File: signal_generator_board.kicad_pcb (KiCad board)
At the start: 2 copper layers, 100 x 43.8 mm, 50 parts, among them IC1 CD4001, IC2 CD4017, IC3 CD4017, IC4 MAX297, IC5 MCP6024, IC6 NE5532, IC7 ATMEG328PU, IC8 LTC6903/4, IC9 AD5207, P1 CONN_10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

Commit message: v1.0
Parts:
- removed IC2, IC3: CD4017, SO16E
- removed IC4: MAX297, SO8E
- removed IC9: AD5207, TSSOP14
- removed R4: 2.5Meg, SM1206
- removed R5: 1.5Meg, SM1206
- removed R6, R7: 10k, SM1206
- removed RES1: 16MHz, PIN_ARRAY_3X1
- added C17: 0.1uF, SM0603, F.Cu at (106.5, 61.9)
- added C18: 0.1uF, SM0603, F.Cu at (106.0, 45.6)
- added JP1: USB_POWER, PIN_ARRAY_2X1, F.Cu at (110.8, 31.7)
- added Q1: 2N7002, SOT23, F.Cu at (91.7, 47.0)
- added U1: 4066, SO14E, F.Cu at (90.5, 57.7)
- added U2: 74LS393, SO14E, F.Cu at (118.2, 58.5)
- added X1: 16MHz, HC-49V, F.Cu at (95.1, 29.6)
- C10, C11: value 1uF -> 22pF
- C12: value 0.1uF -> 1uF; footprint SM0603 -> SM1206
- C13: value 1uF -> 5pF
- C3: value 0.1uF -> 47nF; footprint SM0603 -> SM1206
- C4: value 0.1uF -> 470pF; footprint SM0603 -> SM1206
- C6: value 0.1uF -> 6.8nF; footprint SM0603 -> SM1206
- C7: value 1uF -> 68pF
- IC1: value CD4001 -> AD5206; footprint SO14E -> SO24E
- R2: value 2k -> 1k
- R3: value 3k -> 1Meg
- R8: value 250k -> 25k
- R9: value 1Meg -> 100k
- U3: value RBBB -> TLE2426; footprint RBBB_shield -> SO8E
- moved D1 89.3 mm to (29.4, 60.2), turned to 0 degrees
- moved R10 89.2 mm to (29.7, 57.6), turned to 0 degrees
- moved C10 45.0 mm to (105.1, 29.9)
- moved P6 42.9 mm to (81.9, 29.7), turned to 180 degrees
- moved R3 34.2 mm to (102.5, 29.9), turned to 90 degrees
- moved C3 32.4 mm to (86.8, 64.6), turned to 90 degrees
- moved SW1 32.4 mm to (120.2, 37.3), turned to 270 degrees
- moved U3 31.9 mm to (109.9, 64.3), turned to 0 degrees
- moved C11 31.4 mm to (87.7, 29.8)
- moved C8 23.3 mm to (120.7, 62.8)
- moved R1 21.4 mm to (118.8, 31.1)
- moved C14 20.7 mm to (113.6, 66.6), turned to 90 degrees
- moved C4 17.6 mm to (89.5, 64.6), turned to 90 degrees
- moved C5 16.4 mm to (84.7, 57.7), turned to 90 degrees
- moved IC5 16.1 mm to (100.7, 64.1)
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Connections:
- net +3.3V_SCL renamed N-0000016
- net +3.3V_SDA renamed N-0000013
- C10 pad 1: N-0000081 -> GND
- C10 pad 2: N-0000082 -> N-0000071
- C11 pad 1: N-0000082 -> GND
- C11 pad 2: 5Vp-p_WAVEOUT -> N-0000072
- C12 pad 1: N-0000048 -> N-0000040
- C12 pad 2: G -> 5Vp-p_WAVEOUT
- C14 pad 2: G -> GND
- C15 pad 2: G -> GND
- C16 pad 1: +12V -> GND
- C16 pad 2: G -> +12V
- C2 pad 2: G -> GND
- C3 pad 1: +5V -> C1A
- C3 pad 2: G -> N-000006
- C4 pad 1: +5V -> C1A
- C4 pad 2: G -> N-000001
- C5 pad 1: +5V -> GND
- C5 pad 2: G -> +5V
- C6 pad 1: +5V -> C2A
- C6 pad 2: G -> N-000004
- C7 pad 1: N-0000040 -> C2A
- C8 pad 1: VGND -> GND
- C8 pad 2: G -> +5V
- C9 pad 2: G -> GND
- D1 pad 2: G -> GND
- IC1 pad 1: N-0000078 -> N-0000025
- IC1 pad 10: (no net) -> N-0000020
- IC1 pad 11: (no net) -> N-0000025
- IC1 pad 12: G -> N-0000025
- IC1 pad 13: G -> C1A
- IC1 pad 14: +5V -> C2A
- IC1 pad 2: N-0000083 -> N-0000041
- IC1 pad 3: N-0000079 -> VGND
- IC1 pad 4: N-0000083 -> GND
- IC1 pad 5: N-0000079 -> D3
- IC1 pad 6: /CLK -> +5V
- IC1 pad 7: G -> D11/MOSI
- IC1 pad 8: G -> D13/SCK
- IC1 pad 9: G -> GND
- IC5 pad 1: N-0000082 -> C1B
- IC5 pad 10: VGND -> N-0000041
- IC5 pad 11: G -> GND
- IC5 pad 13: N-0000063 -> N-0000020
- IC5 pad 14: N-0000063 -> N-0000025
- IC5 pad 2: N-0000081 -> C1B
- IC5 pad 3: (no net) -> C2A
- IC5 pad 5: N-0000048 -> N-0000042
- IC5 pad 6: VGND -> N-0000044
- IC5 pad 7: VGND -> N-0000044
- IC5 pad 8: N-0000061 -> 5Vp-p_WAVEOUT
- IC5 pad 9: N-0000061 -> 5Vp-p_WAVEOUT
- IC6 pad 3: G -> GND
- IC6 pad 5: G -> GND
- IC7 pad 10: N-0000021 -> N-0000072
- IC7 pad 11: D5 -> (no net)
- IC7 pad 12: D6 -> (no net)
- IC7 pad 13: D7 -> (no net)
- IC7 pad 14: D8 -> (no net)
- IC7 pad 15: D9 -> (no net)
- IC7 pad 16: D10 -> (no net)
- IC7 pad 20: G -> +5V
- IC7 pad 21: AR -> (no net)
- IC7 pad 22: +5V -> GND
- IC7 pad 23: A0 -> (no net)
- IC7 pad 24: A1 -> (no net)
- IC7 pad 25: A2 -> (no net)
- IC7 pad 26: A3 -> (no net)
- IC7 pad 8: G -> GND
- IC7 pad 9: N-0000019 -> N-0000071
- IC8 pad 1: G -> GND
- IC8 pad 6: /CLK -> N-0000045
- P1 pad 3: G -> GND
- P1 pad 8: G -> N-0000015
- P1 pad 9: +3.3V -> N-0000014
- P2 pad 3: +3.3V -> (no net)
- P2 pad 5: G -> GND
- P2 pad 6: G -> GND
- P2 pad 7: G -> GND
- P2 pad 8: G -> GND
- P3 pad 1: G -> GND
- P3 pad 3: +5V -> +5V_USB
- P4 pad 3: G -> GND
- P4 pad 8: G -> N-0000015
- P4 pad 9: +3.3V -> N-0000014
- P5 pad 1: G -> GND
- P6 pad 6: G -> GND
- R2 pad 1: N-0000069 -> +5V
- R2 pad 2: N-0000059 -> N-000007
- R3 pad 1: N-0000059 -> N-0000071
- R3 pad 2: VGND -> N-0000072
- R8 pad 1: 5Vp-p_WAVEOUT -> N-0000040
- SW1 pad 2: G -> GND
- SW1 pad 4: G -> GND
- U3 pad 1: RST -> VGND
- U3 pad 2: G -> GND
- U3 pad 4: TX -> (no net)
- U3 pad 5: RX -> (no net)
- U3 pad 6: D2 -> (no net)
- U3 pad 7: D3 -> (no net)
- U3 pad 8: D4 -> N-0000038
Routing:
- net G: track 216.7 -> 0.00 mm, vias 7 -> 0
- net GND: track 0.00 -> 126.3 mm, vias 0 -> 5
- net +3.3V: track 81.9 -> 0.00 mm
- net N-0000014: track 0.00 -> 49.3 mm
- net /CLK: track 46.2 -> 0.00 mm
- net N-0000015: track 0.00 -> 43.3 mm
- net C1B: track 0.00 -> 39.6 mm, vias 0 -> 4
- net N-0000083: track 38.4 -> 0.00 mm, vias 2 -> 0
- net D4: track 2.54 -> 39.8 mm, vias 0 -> 2
- net N-0000025: track 0.00 -> 34.2 mm, vias 0 -> 2
- net N-0000020: track 0.00 -> 33.7 mm, vias 0 -> 4
- net C1A: track 0.00 -> 31.7 mm, vias 0 -> 2
- net C2A: track 0.00 -> 30.7 mm, vias 0 -> 3
- net N-0000081: track 30.5 -> 0.00 mm
- net 5Vp-p_WAVEOUT: track 27.9 -> 57.5 mm
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- added copper zone on B.Cu, net GND
- added copper zone on F.Cu, net GND
- removed copper zone on B.Cu, net G
- removed copper zone on F.Cu, net G
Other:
- board size 100 x 43.8 mm -> 100 x 44.8 mm
- board text added: "ICSP"
- board text added: "OUT_TO_AMP"

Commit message: Add missing parts to BOM
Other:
- board text added: "Signal Generator Board v1.0.1 http://microfluidics.utoronto.ca/dropbot"
- board text removed: "Signal Generator Board v1.0 http://microfluidics.utoronto.ca/dropbot"
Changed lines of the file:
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@@
     (visible_elements 7FFFFFFF)
     (pcbplotparams
-      (layerselection 284196865)
+      (layerselection 2097152)
       (usegerberextensions true)
       (excludeedgelayer true)
@@
     (effects (font (size 0.8 0.8) (thickness 0.2)))
   )
-  (gr_text "Signal Generator\nBoard v1.0\nhttp://microfluidics.utoronto.ca/dropbot" (at 26.4795 51.562) (layer F.SilkS)
+  (gr_text "Signal Generator\nBoard v1.0.1\nhttp://microfluidics.utoronto.ca/dropbot" (at 26.4795 51.562) (layer F.SilkS)
     (effects (font (size 1.1 0.9) (thickness 0.1875)) (justify left))
   )

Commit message: Fix link on BOM
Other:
- board text added: "Signal Generator Board v1.0.2 http://microfluidics.utoronto.ca/dropbot"
- board text removed: "Signal Generator Board v1.0.1 http://microfluidics.utoronto.ca/dropbot"
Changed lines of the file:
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@@
     (effects (font (size 0.8 0.8) (thickness 0.2)))
   )
-  (gr_text "Signal Generator\nBoard v1.0.1\nhttp://microfluidics.utoronto.ca/dropbot" (at 26.4795 51.562) (layer F.SilkS)
+  (gr_text "Signal Generator\nBoard v1.0.2\nhttp://microfluidics.utoronto.ca/dropbot" (at 26.4795 51.562) (layer F.SilkS)
     (effects (font (size 1.1 0.9) (thickness 0.1875)) (justify left))
   )

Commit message: Add paste and pos files
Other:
- board text added: "Signal Generator Board v1.0 http://microfluidics.utoronto.ca/dropbot"
- board text removed: "Signal Generator Board v1.0.2 http://microfluidics.utoronto.ca/dropbot"
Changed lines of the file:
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@@
     (visible_elements 7FFFFFFF)
     (pcbplotparams
-      (layerselection 2097152)
+      (layerselection 284983297)
       (usegerberextensions true)
       (excludeedgelayer true)
@@
     (effects (font (size 0.8 0.8) (thickness 0.2)))
   )
-  (gr_text "Signal Generator\nBoard v1.0.2\nhttp://microfluidics.utoronto.ca/dropbot" (at 26.4795 51.562) (layer F.SilkS)
+  (gr_text "Signal Generator\nBoard v1.0\nhttp://microfluidics.utoronto.ca/dropbot" (at 26.4795 51.562) (layer F.SilkS)
     (effects (font (size 1.1 0.9) (thickness 0.1875)) (justify left))
   )

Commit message: Change C4 and C7 (update BOM)
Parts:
- C4: value 470pF -> 4.7nF
- C7: value 68pF -> 680pF
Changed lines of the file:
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@@
       (effects (font (size 0.762 0.762) (thickness 0.127)))
     )
-    (fp_text value 470pF (at 0 0 90) (layer F.SilkS) hide
+    (fp_text value 4.7nF (at 0 0 90) (layer F.SilkS) hide
       (effects (font (size 0.762 0.762) (thickness 0.127)))
     )
@@
       (effects (font (size 0.762 0.762) (thickness 0.127)))
     )
-    (fp_text value 68pF (at 0 0 180) (layer F.SilkS) hide
+    (fp_text value 680pF (at 0 0 180) (layer F.SilkS) hide
       (effects (font (size 0.762 0.762) (thickness 0.127)))
     )

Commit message: Fix #37
Remove DC bias from 5 Vpk-pk output
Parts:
- moved C12 0.23 mm to (82.5, 59.9), turned to 90 degrees
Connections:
- C12 pad 1: N-0000040 (its old number) -> N-0000039
- IC5 pad 8: 5Vp-p_WAVEOUT -> N-0000039
- IC5 pad 9: 5Vp-p_WAVEOUT -> N-0000039
- R8 pad 1: N-0000040 (its old number) -> 5Vp-p_WAVEOUT
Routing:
- net N-0000039: track 0.00 -> 30.7 mm
- net 5Vp-p_WAVEOUT: track 57.5 -> 33.8 mm, vias 1 -> 3
- net N-0000040 (its old number): track 11.5 -> 0.00 mm, vias 2 -> 0
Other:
- board text added: "Signal Generator Board v1.1 http://microfluidics.utoronto.ca/dropbot"
- board text removed: "Signal Generator Board v1.0 http://microfluidics.utoronto.ca/dropbot"

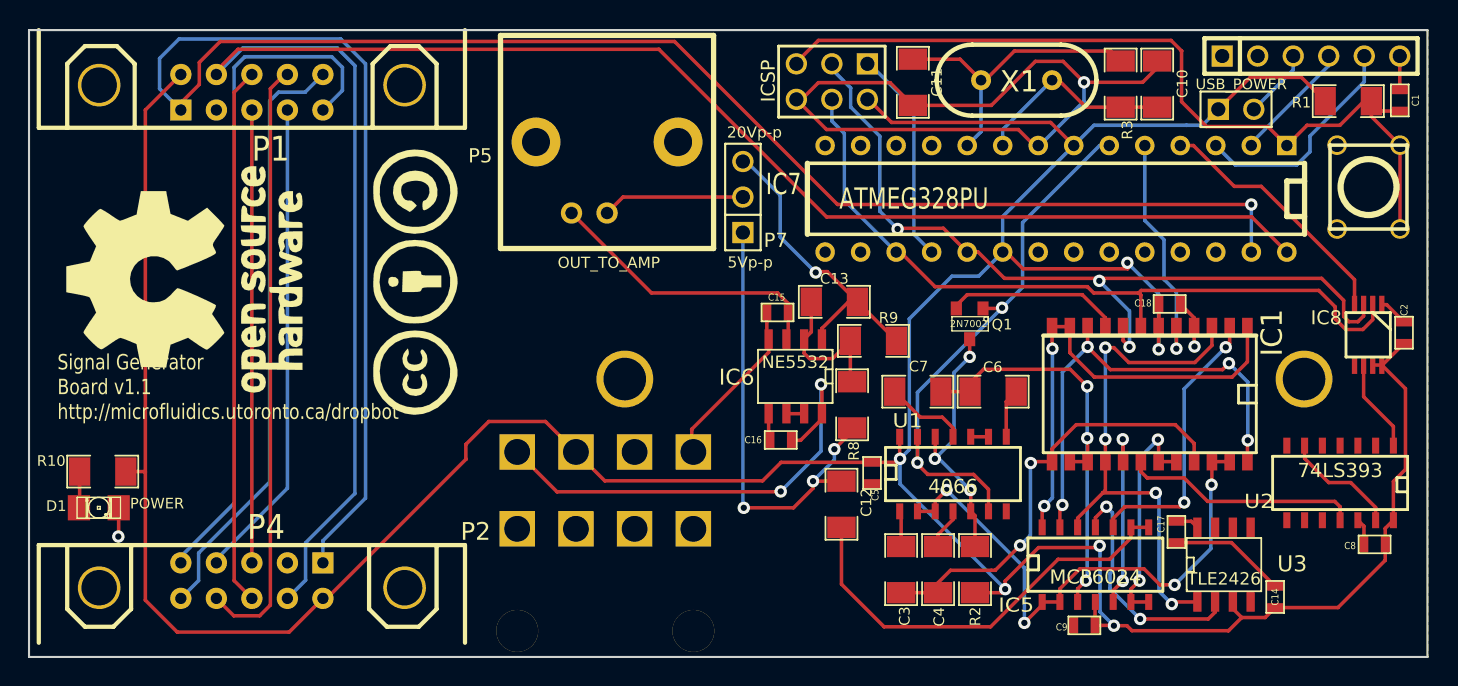
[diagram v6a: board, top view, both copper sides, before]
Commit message: Add ISP prgramming, replace 0603 caps with 1206, ...
* add polarity labels to LEDs
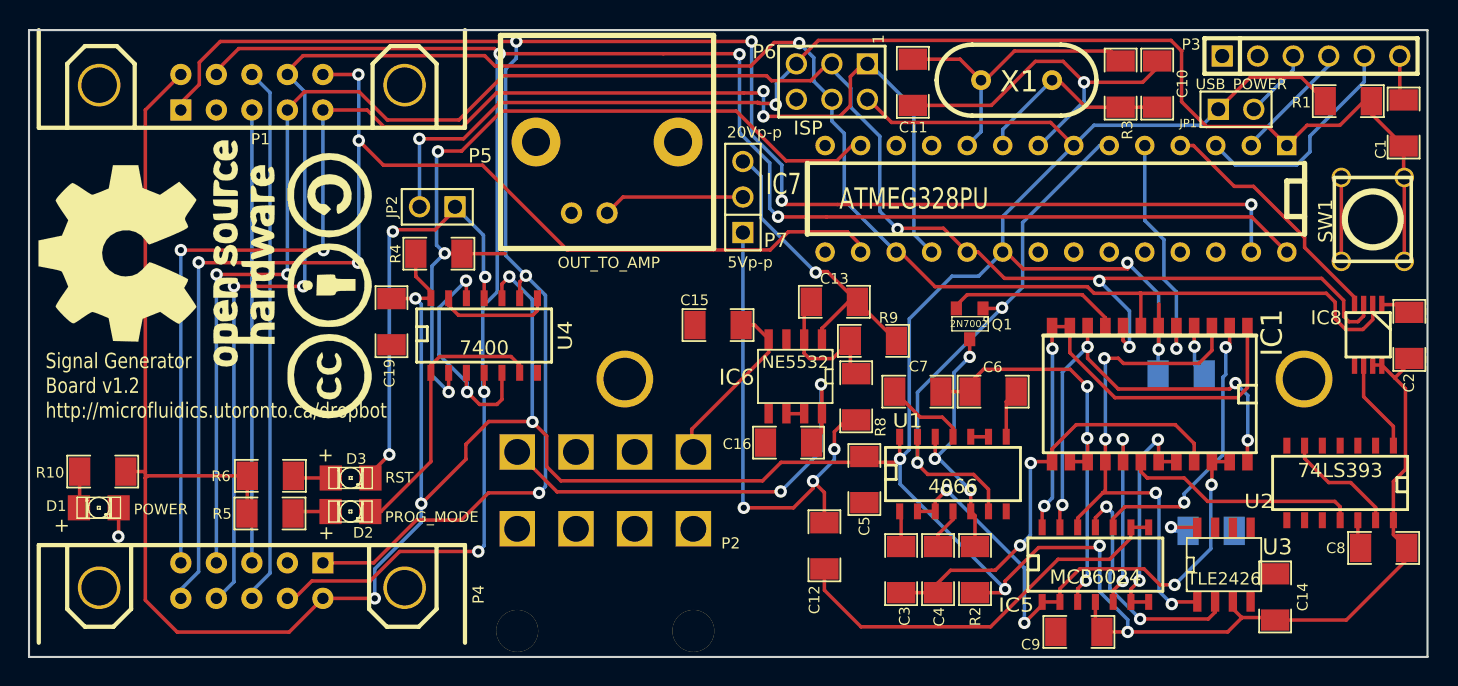
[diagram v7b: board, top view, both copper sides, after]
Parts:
- added C19: 0.1uF, SM1206, F.Cu at (50.4, 46.9)
- added D2: PROG_MODE, LED-1206, F.Cu at (47.4, 60.5)
- added D3: RST, LED-1206, F.Cu at (47.4, 58.1)
- added JP2: JUMPER, PIN_ARRAY_2X1, F.Cu at (53.6, 38.7)
- added R4: 1k, SM1206, F.Cu at (53.8, 42.0)
- added R5: 1k, SM1206, F.Cu at (41.7, 60.6)
- added R6: 1k, SM1206, F.Cu at (41.7, 57.9)
- added U4: 7400, SO14E, F.Cu at (57.0, 47.8)
- C1, C14, C15, C16, C2, C5, C8, C9: footprint SM0603 -> SM1206
- C17, C18: footprint SM0603 -> SM1206; moved to B.Cu
- R10: value 374 -> 1k
- moved G*** 6.14 mm to (45.9, 44.3)
- moved C18 5.11 mm to (106.8, 50.7)
- moved C15 4.35 mm to (73.7, 47.1), turned to 180 degrees
- moved C12 3.21 mm to (81.3, 62.9)
- moved G*** 2.72 mm to (33.6, 42.0)
- moved C17 2.49 mm to (109.0, 61.8), turned to 180 degrees
- moved SW1 2.33 mm to (120.5, 39.6)
- moved C1 1.64 mm to (122.8, 32.7)
- moved C5 0.72 mm to (84.2, 58.2)
- moved C8 0.70 mm to (121.3, 63.1)
- moved R8 0.64 mm to (83.6, 52.3)
- moved C9 0.61 mm to (99.5, 69.1)
- moved C16 0.59 mm to (78.8, 55.5)
- moved C2 0.42 mm to (123.2, 47.9)
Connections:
- C14 pad 1: +5V -> VCC
- C18 pad 1: +5V -> VCC
- C2 pad 1: +5V -> VCC
- C5 pad 2: +5V -> VCC
- C8 pad 2: +5V -> VCC
- C9 pad 1: +5V -> VCC
- IC1 pad 6: +5V -> VCC
- IC5 pad 4: +5V -> VCC
- IC7 pad 13: (no net) -> D7
- IC7 pad 16: (no net) -> D10/SS
- IC7 pad 20: +5V -> VCC
- IC7 pad 7: +5V -> VCC
- IC8 pad 7: +5V -> VCC
- IC8 pad 8: +5V -> VCC
- JP1 pad 1: +5V -> VCC
- P1 pad 10: N-0000013 (its old number) -> D10/SS
- P1 pad 2: +5V -> VCC
- P1 pad 7: N-0000016 -> D13/SCK
- P1 pad 8: N-0000015 (its old number) -> D11/MOSI
- P1 pad 9: N-0000014 -> D12/MISO
- P2 pad 2: +5V -> (no net)
- P4 pad 10: N-0000013 (its old number) -> D10/SS
- P4 pad 2: +5V -> VCC
- P4 pad 7: N-0000016 -> D13/SCK
- P4 pad 8: N-0000015 (its old number) -> D11/MOSI
- P4 pad 9: N-0000014 -> D12/MISO
- P6 pad 2: +5V -> VCC
- R1 pad 2: +5V -> VCC
- R10 pad 2: +5V -> VCC
- R2 pad 1: +5V -> VCC
- U1 pad 14: +5V -> VCC
- U2 pad 14: +5V -> VCC
- U3 pad 3: +5V -> VCC
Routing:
- net VCC: track 0.00 -> 317.2 mm, vias 0 -> 11
- net +5V: track 265.2 -> 0.00 mm, vias 6 -> 0
- net D10/SS: track 0.00 -> 92.6 mm, vias 0 -> 4
- net D12/MISO: track 15.5 -> 103.4 mm, vias 0 -> 4
- net D11/MOSI: track 53.7 -> 140.6 mm, vias 0 -> 3
- net D13/SCK: track 59.2 -> 139.0 mm, vias 3 -> 5
- net D7: track 0.00 -> 57.4 mm, vias 0 -> 3
- net GND: track 126.3 -> 74.2 mm
- net N-0000014: track 49.3 -> 0.00 mm
- net N-0000015 (its old number): track 43.3 -> 0.00 mm
- net N-0000013 (its old number): track 42.8 -> 0.00 mm
- net RST: track 60.8 -> 96.0 mm, vias 0 -> 2
- net N-0000016: track 34.5 -> 0.00 mm
- net N-0000031: track 0.00 -> 31.1 mm, vias 0 -> 3
- net N-0000028: track 0.00 -> 20.1 mm
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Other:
- board text added: "+"
- board text added: "1"
- board text added: "ISP"
- board text added: "Signal Generator Board v1.2 http://microfluidics.utoronto.ca/dropbot"
- board text removed: "ICSP"
- board text removed: "Signal Generator Board v1.1 http://microfluidics.utoronto.ca/dropbot"

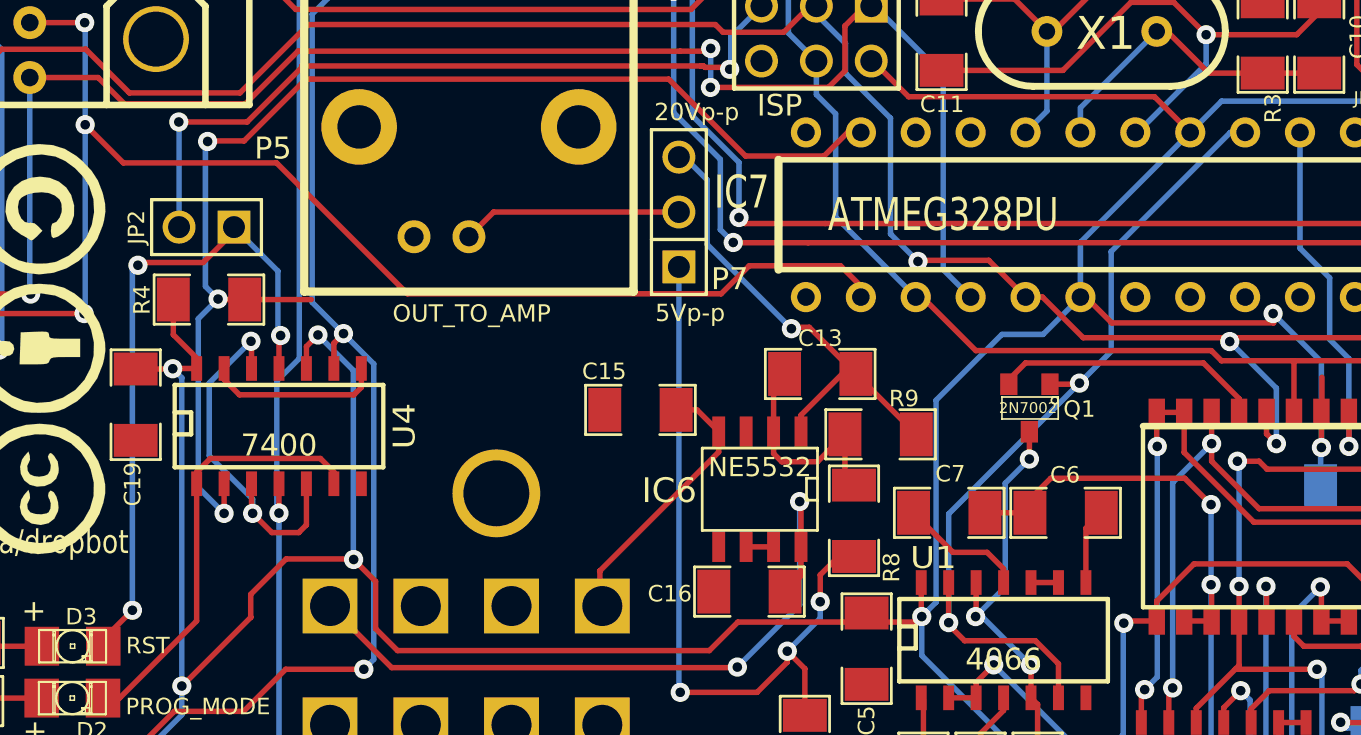
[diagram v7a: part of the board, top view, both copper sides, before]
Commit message: Fix BOM, labels, modify to use soft/bitbanged SPI
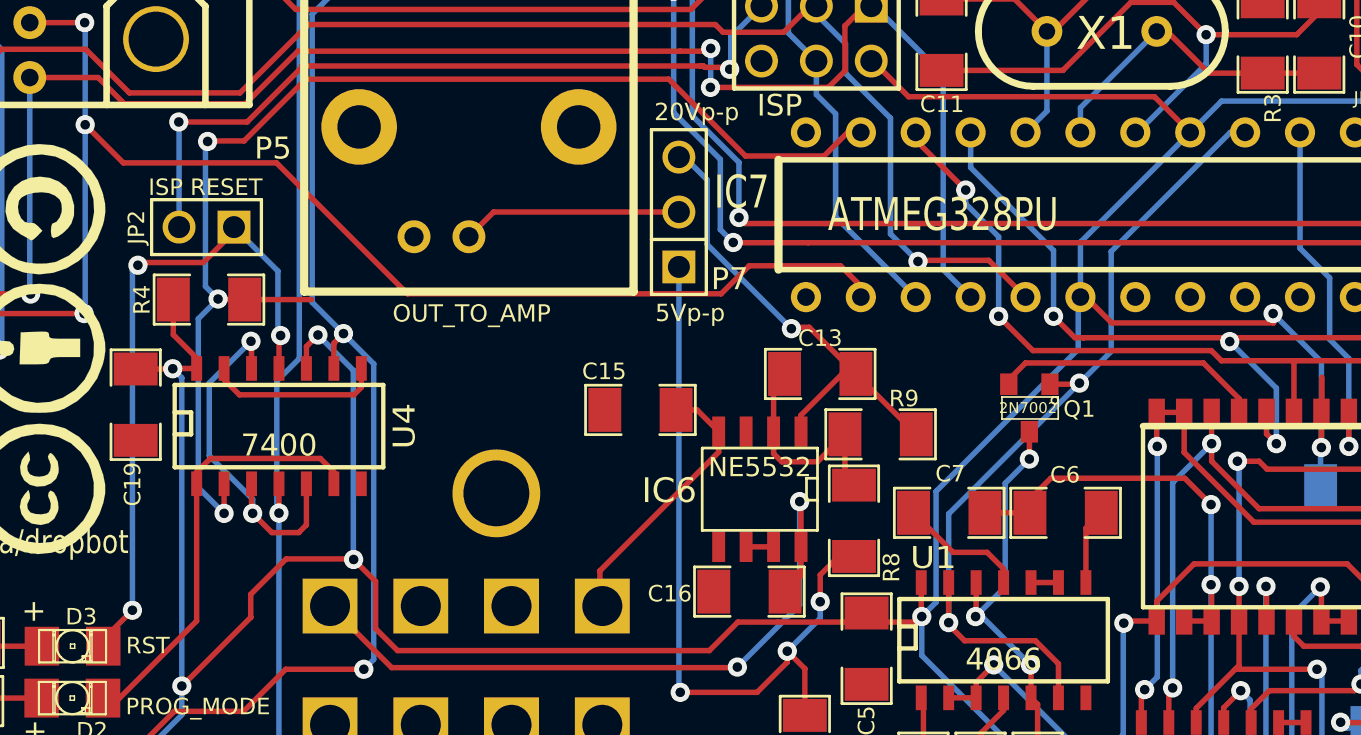
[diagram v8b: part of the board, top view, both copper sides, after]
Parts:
- JP2: value JUMPER -> ISP RESET
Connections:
- net D2 renamed D2/LTC6904_SS
- net D3 renamed D3/AD5206_SS
- net D4 renamed D4/FREQ_RANGE
- net D7 renamed D7/ISP_ENABLE
- IC1 pad 7: D11/MOSI -> D6/S_MOSI
- IC1 pad 8: D13/SCK -> D5/S_SCK
- IC7 pad 11: (no net) -> D5/S_SCK
- IC7 pad 12: (no net) -> D6/S_MOSI
- IC8 pad 2: D11/MOSI -> D6/S_MOSI
- IC8 pad 3: D13/SCK -> D5/S_SCK
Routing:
- net D5/S_SCK: track 0.00 -> 48.0 mm, vias 0 -> 3
- net D6/S_MOSI: track 0.00 -> 46.8 mm, vias 0 -> 2
- net D11/MOSI: track 140.6 -> 100.0 mm
- net D13/SCK: track 139.0 -> 99.5 mm, vias 5 -> 3
- net VCC: track 317.2 -> 316.1 mm
